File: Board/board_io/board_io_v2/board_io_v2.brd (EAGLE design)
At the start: 90.2 x 55.9 mm, 38 parts, among them IC1 LD117AS33TR, IC2 LD117AS18TR, IC3 FT232RL

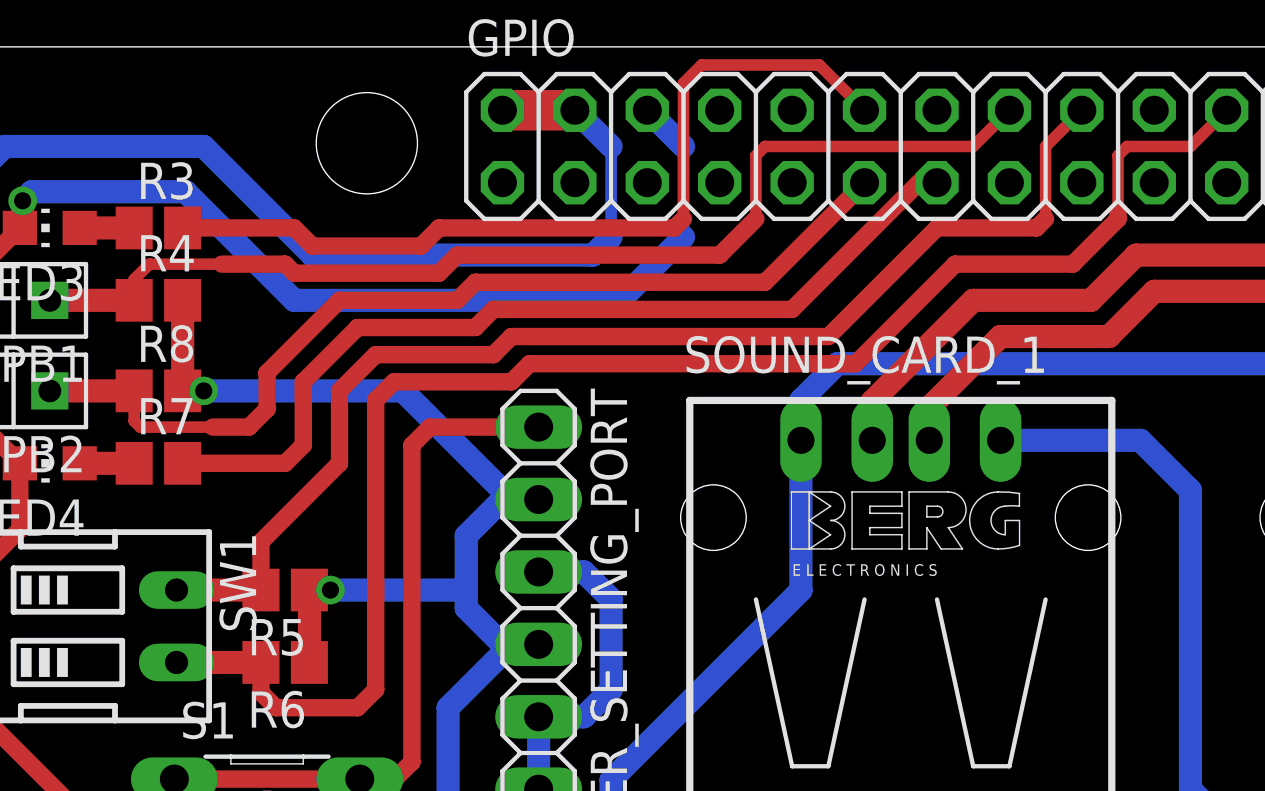
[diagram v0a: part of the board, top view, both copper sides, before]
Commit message: update io board and add interface code
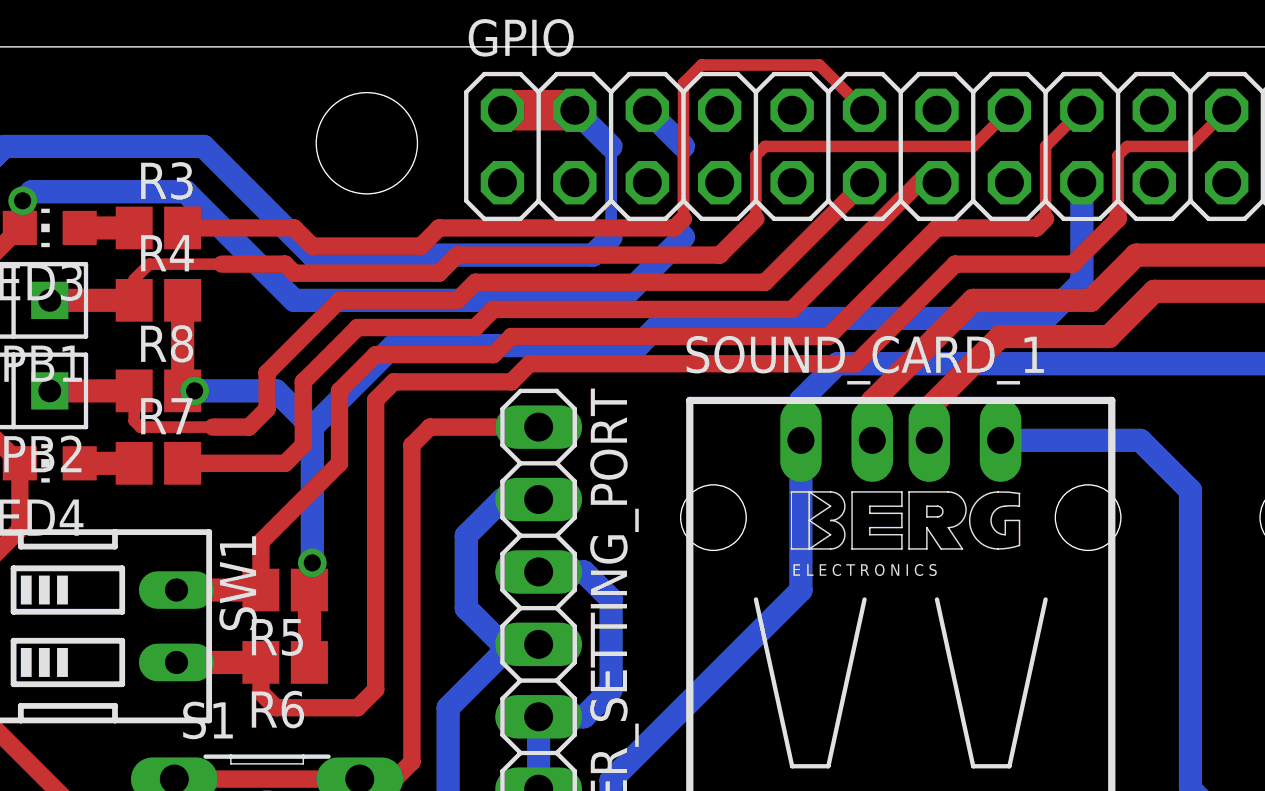
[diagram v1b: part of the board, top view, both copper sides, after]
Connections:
- net 3V3: no longer R4.2, R5.1, R6.1, R8.2
- net RPI_3V3: now also GPIO.17, R4.2, R5.1, R6.1, R8.2; no longer GPIO.1
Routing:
- net RPI_3V3: track 0.00 -> 49.1 mm, vias 0 -> 2
- net 3V3: track 115.9 -> 91.5 mm, vias 2 -> 0
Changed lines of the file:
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@@
 <contactref element="VOCODER_SETTING_PORT" pad="2"/>
 <contactref element="VOCODER_SETTING_PORT" pad="4"/>
-<contactref element="R4" pad="2"/>
-<contactref element="R6" pad="1"/>
-<contactref element="R5" pad="1"/>
-<contactref element="R8" pad="2"/>
 <wire x1="24.4475" y1="12.04" x2="28.2825" y2="12.04" width="0.8128" layer="16"/>
 <wire x1="28.2825" y1="12.04" x2="29.5275" y2="10.795" width="0.8128" layer="16"/>
@@
 <wire x1="45.4025" y1="14.605" x2="53.0225" y2="22.225" width="0.8128" layer="16"/>
 <wire x1="53.0225" y1="22.225" x2="55.245" y2="22.225" width="0.8128" layer="16"/>
-<wire x1="9.525" y1="40.005" x2="8.5725" y2="40.005" width="0.8128" layer="16"/>
-<wire x1="8.5725" y1="40.005" x2="8.255" y2="40.005" width="0.8128" layer="16"/>
+<wire x1="9.525" y1="40.005" x2="8.255" y2="40.005" width="0.8128" layer="16"/>
 <wire x1="8.255" y1="40.005" x2="6.985" y2="38.735" width="0.8128" layer="16"/>
-<wire x1="6.985" y1="38.735" x2="6.985" y2="36.83" width="0.8128" layer="16"/>
-<wire x1="6.985" y1="36.83" x2="6.985" y2="36.195" width="0.8128" layer="16"/>
+<wire x1="6.985" y1="38.735" x2="6.985" y2="36.195" width="0.8128" layer="16"/>
 <wire x1="6.985" y1="36.195" x2="8.255" y2="34.925" width="0.8128" layer="16"/>
 <wire x1="8.255" y1="34.925" x2="8.5725" y2="34.925" width="0.8128" layer="16"/>
 <wire x1="8.5725" y1="34.925" x2="9.525" y2="34.925" width="0.8128" layer="16"/>
-<wire x1="1.485" y1="36.83" x2="1.485" y2="34.29" width="0.8128" layer="1"/>
-<wire x1="-2.96" y1="46.99" x2="-2.96" y2="43.815" width="0.8128" layer="1"/>
-<wire x1="1.485" y1="36.83" x2="2.2225" y2="36.83" width="0.6096" layer="1"/>
-<via x="2.2225" y="36.83" extent="1-16" drill="0.6" shape="octagon"/>
-<wire x1="2.2225" y1="36.83" x2="6.985" y2="36.83" width="0.8128" layer="16"/>
-<wire x1="-2.96" y1="43.815" x2="-2.2225" y2="43.815" width="0.6096" layer="1"/>
-<via x="-2.2225" y="43.815" extent="1-16" drill="0.6" shape="octagon"/>
-<wire x1="-2.2225" y1="43.815" x2="4.7625" y2="43.815" width="0.8128" layer="16"/>
-<wire x1="4.7625" y1="43.815" x2="8.5725" y2="40.005" width="0.8128" layer="16"/>
 <wire x1="6.6675" y1="10.4775" x2="4.1275" y2="13.0175" width="0.8128" layer="16"/>
 <wire x1="4.1275" y1="13.0175" x2="4.1275" y2="21.59" width="0.8128" layer="16"/>
@@
 </signal>
 <signal name="RPI_3V3">
-<contactref element="GPIO" pad="1"/>
+<contactref element="R8" pad="2"/>
+<contactref element="R4" pad="2"/>
+<contactref element="R5" pad="1"/>
+<contactref element="R6" pad="1"/>
+<contactref element="GPIO" pad="17"/>
+<wire x1="-2.96" y1="46.99" x2="-2.96" y2="43.815" width="0.8128" layer="1"/>
+<wire x1="1.485" y1="36.83" x2="1.485" y2="34.29" width="0.8128" layer="1"/>
+<wire x1="-2.96" y1="43.815" x2="-2.54" y2="43.815" width="0.8128" layer="1"/>
+<via x="-2.54" y="43.815" extent="1-16" drill="0.6" shape="octagon"/>
+<wire x1="-2.54" y1="43.815" x2="0.3175" y2="43.815" width="0.8128" layer="16"/>
+<wire x1="0.3175" y1="43.815" x2="1.5875" y2="42.545" width="0.8128" layer="16"/>
+<wire x1="1.5875" y1="42.545" x2="1.5875" y2="37.7825" width="0.8128" layer="16"/>
+<via x="1.5875" y="37.7825" extent="1-16" drill="0.6" shape="octagon"/>
+<wire x1="1.5875" y1="37.7825" x2="1.5875" y2="36.9325" width="0.8128" layer="1"/>
+<wire x1="1.5875" y1="36.9325" x2="1.485" y2="36.83" width="0.8128" layer="1"/>
+<wire x1="28.575" y1="51.1175" x2="28.575" y2="47.625" width="0.8128" layer="16"/>
+<wire x1="28.575" y1="47.625" x2="27.305" y2="46.355" width="0.8128" layer="16"/>
+<wire x1="27.305" y1="46.355" x2="13.97" y2="46.355" width="0.8128" layer="16"/>
+<wire x1="13.97" y1="46.355" x2="13.0175" y2="45.4025" width="0.8128" layer="16"/>
+<wire x1="13.0175" y1="45.4025" x2="4.445" y2="45.4025" width="0.8128" layer="16"/>
+<wire x1="4.445" y1="45.4025" x2="1.5875" y2="42.545" width="0.8128" layer="16"/>
 </signal>
 <signal name="DSP_RESET">
